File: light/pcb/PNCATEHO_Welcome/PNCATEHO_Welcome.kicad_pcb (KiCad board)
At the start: 2 copper layers, 85.6 x 54 mm, 53 parts, among them J1 USB_C_Receptacle_USB2.0, SW11 Boot, SW12 Reset, U1 RP2040, U2 RT9013-33GB, U3 W25Q32JVSSIQ, U4 USBLC6-2SC6, Y1 12MHz

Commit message: fix silc
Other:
- board text added: "pcb: turtle & inpudiy"
- board text removed: "pcb: turtle & inpdiy"

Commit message: add led
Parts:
- removed R8: 10k, PNCATEHO:R_0805_2012Metric_Pad1.20x1.40mm_HandSolder
- removed REF**: CreditCardPads, PNCATEHO:CreditCardPads
- added D10: LED_WS2812-2020, PNCATEHO:WS2812-2020-2.00mmx2.20mm, F.Cu at (156.6, 99.6)
- added D11: LED_WS2812-2020, PNCATEHO:WS2812-2020-2.00mmx2.20mm, F.Cu at (156.7, 116.7)
- added D12: LED_WS2812-2020, PNCATEHO:WS2812-2020-2.00mmx2.20mm, F.Cu at (173.7, 116.7)
- added D3: LED_WS2812-2020, PNCATEHO:WS2812-2020-2.00mmx2.20mm, F.Cu at (105.9, 82.8)
- added D4: LED_WS2812-2020, PNCATEHO:WS2812-2020-2.00mmx2.20mm, F.Cu at (122.8, 82.8)
- added D5: LED_WS2812-2020, PNCATEHO:WS2812-2020-2.00mmx2.20mm, F.Cu at (139.8, 82.8)
- added D6: LED_WS2812-2020, PNCATEHO:WS2812-2020-2.00mmx2.20mm, F.Cu at (156.7, 82.8)
- added D7: LED_WS2812-2020, PNCATEHO:WS2812-2020-2.00mmx2.20mm, F.Cu at (105.9, 99.8)
- added D8: LED_WS2812-2020, PNCATEHO:WS2812-2020-2.00mmx2.20mm, F.Cu at (122.8, 99.8)
- added D9: LED_WS2812-2020, PNCATEHO:WS2812-2020-2.00mmx2.20mm, F.Cu at (139.8, 99.8)
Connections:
- net /RP2040_D+ renamed Net-(U1-USB_DP)
- net /RP2040_D- renamed Net-(U1-USB_DM)
- net USB_PROTECTED_D+ renamed USB_DP
- net USB_PROTECTED_D- renamed USB_DM
- U1 pad 36: unconnected-(U1-GPIO24-Pad36) -> LED

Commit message: fix sh
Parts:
- D10, D11, D12, D3, D4, D5, D6, D7, D8, D9: value LED_WS2812-2020 -> ~
- moved D3 50.9 mm to (156.7, 82.8)
- moved D6 50.9 mm to (105.9, 82.8)
- moved D4 16.9 mm to (139.8, 82.8)
- moved D5 16.9 mm to (122.8, 82.8)
- moved D10 0.21 mm to (156.7, 99.8)
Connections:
- D11 pad 1: Net-(D10-DI) -> Net-(D11-DO)
- D11 pad 3: Net-(D11-DI) -> Net-(D10-DO)
- D12 pad 1: Net-(D11-DI) -> unconnected-(D12-DO-Pad1)
- D12 pad 3: unconnected-(D12-DI-Pad3) -> Net-(D11-DO)
- D3 pad 3: Net-(D3-DI) -> LED
- D4 pad 1: Net-(D3-DI) -> Net-(D4-DO)
- D4 pad 3: Net-(D4-DI) -> Net-(D3-DO)
- D5 pad 1: Net-(D4-DI) -> Net-(D5-DO)
- D5 pad 3: Net-(D5-DI) -> Net-(D4-DO)
- D6 pad 1: LED -> Net-(D6-DO)
- D6 pad 3: Net-(D3-DO) -> Net-(D5-DO)
- D7 pad 1: Net-(D5-DI) -> Net-(D7-DO)
- D7 pad 3: Net-(D7-DI) -> Net-(D6-DO)
- D8 pad 1: Net-(D7-DI) -> Net-(D8-DO)
- D8 pad 3: Net-(D8-DI) -> Net-(D7-DO)
- D9 pad 1: Net-(D8-DI) -> Net-(D10-DI)
- D9 pad 3: Net-(D10-DO) -> Net-(D8-DO)

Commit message: PNCATEHO Welcome RGB routing
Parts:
- moved D10 1.54 mm to (157.9, 100.7), turned to 180 degrees
- moved D11 1.54 mm to (157.9, 117.7), turned to 180 degrees
- moved D12 1.54 mm to (174.9, 117.7), turned to 180 degrees
- moved D3 1.54 mm to (157.9, 83.8), turned to 180 degrees
- moved D4 1.54 mm to (141.0, 83.8), turned to 180 degrees
- moved D5 1.54 mm to (124.0, 83.8), turned to 180 degrees
- moved D6 1.54 mm to (107.1, 83.8), turned to 180 degrees
- moved D7 1.54 mm to (107.1, 100.7), turned to 180 degrees
- moved D8 1.54 mm to (124.0, 100.7), turned to 180 degrees
- moved D9 1.54 mm to (141.0, 100.7), turned to 180 degrees
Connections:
- U1 pad 36: LED -> STATE_LED
- U1 pad 37: STATE_LED -> LED
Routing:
- net +5V: track 20.4 -> 219.6 mm, vias 0 -> 8
- net LED: track 0.00 -> 115.4 mm, vias 0 -> 2
- net Net-(D7-DO): track 0.00 -> 24.6 mm, vias 0 -> 2
- net Net-(D8-DO): track 0.00 -> 24.6 mm, vias 0 -> 2
- net Net-(D10-DI): track 0.00 -> 24.6 mm, vias 0 -> 2
- net Net-(D10-DO): track 0.00 -> 24.4 mm, vias 0 -> 2
- net Net-(D6-DO): track 0.00 -> 21.4 mm
- net Net-(D11-DO): track 0.00 -> 21.2 mm
- net Net-(D3-DO): track 0.00 -> 15.9 mm, vias 0 -> 2
- net Net-(D4-DO): track 0.00 -> 15.9 mm, vias 0 -> 2
- net Net-(D5-DO): track 0.00 -> 15.9 mm, vias 0 -> 2
- net ~{RESET}: track 77.2 -> 71.3 mm
- net R1C4: track 50.0 -> 53.2 mm

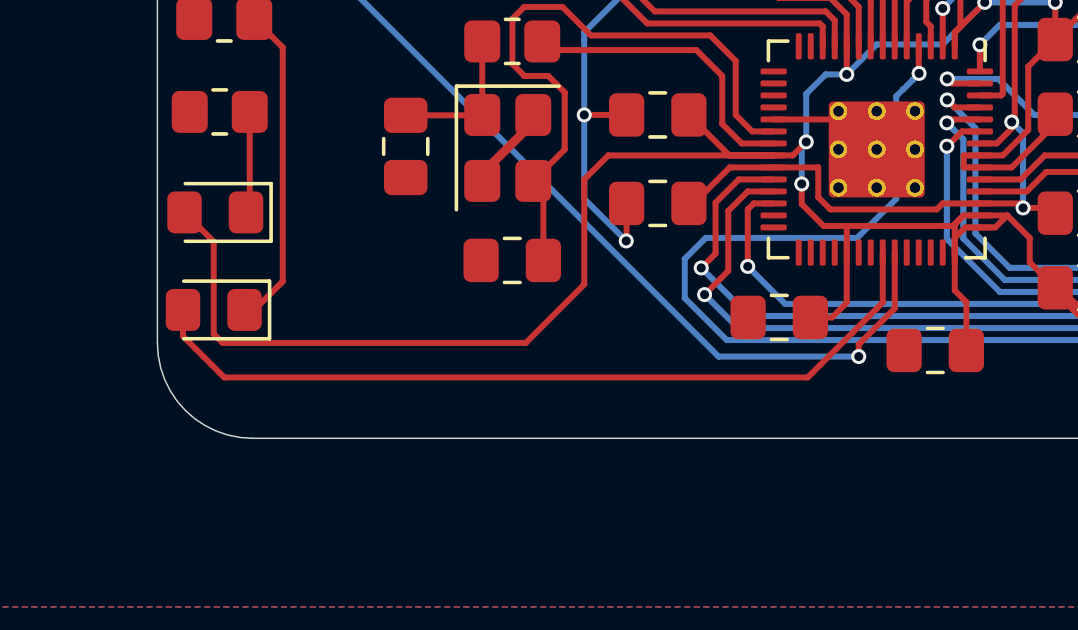
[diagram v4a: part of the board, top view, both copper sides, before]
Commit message: Return state led to GPIO25
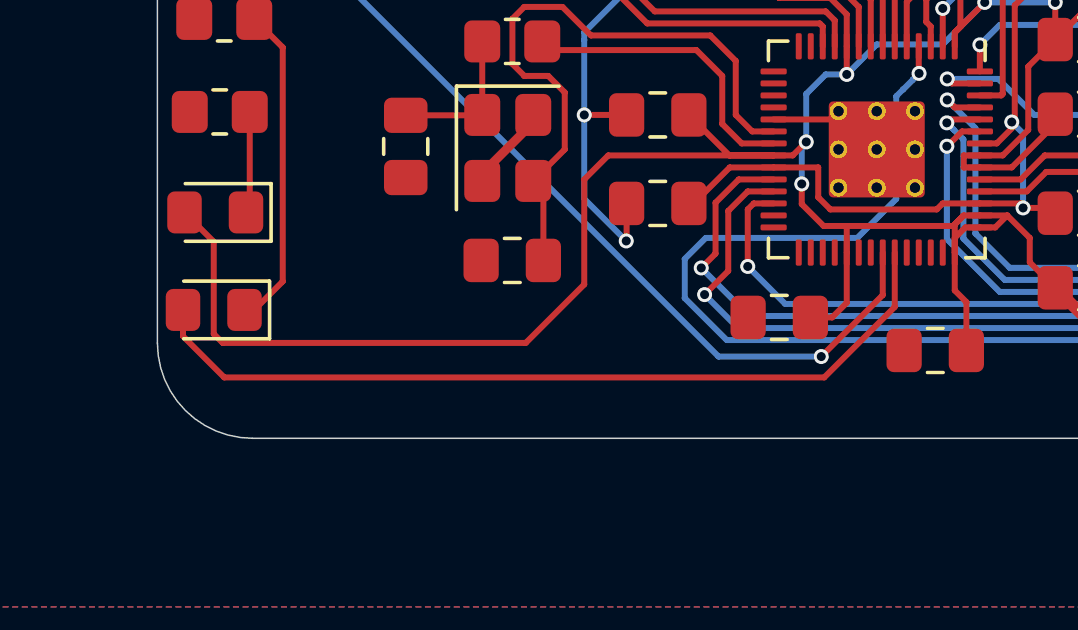
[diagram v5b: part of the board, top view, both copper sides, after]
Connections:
- U1 pad 36: STATE_LED -> LED
- U1 pad 37: LED -> STATE_LED
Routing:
- net LED: track 115.4 -> 114.5 mm

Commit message: update footprint
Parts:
- added G***: LOGO, PNCATEHO:Chip, F.Cu at (170.6, 98.7)
- added J2: Conn_01x10, PNCATEHO:JST_GH_SM10B-GHS-TB_1x10-1MP_P1.25mm_Horizontal, F.Cu at (139.3, 137.7)
- F1: footprint PNCATEHO:Fuse_0805_2012Metric -> PNCATEHO:Fuse_0805_2012Metric_Pad1.15x1.40mm_HandSolder
- TP1: footprint PNCATEHO:TestPoint_Pad_D2.0mm -> PNCATEHO:TestPoint_Pad_1.0x1.0mm
- TP2, TP3, TP4: footprint PNCATEHO:TestPoint_Pad_D2.0mm -> PNCATEHO:TestPoint_Pad_D1.0mm
- U1: footprint PNCATEHO:RP2040-QFN-56 -> PNCATEHO:QFN-56-1EP_7x7mm_P0.4mm_EP3.2x3.2mm_ThermalVias
- U2: footprint PNCATEHO:SOT-23-5_L3.0-W1.7-P0.95-LS2.8-BL -> PNCATEHO:SOT-23-5_HandSoldering
- U3: footprint PNCATEHO:SOIC127P790X216-8N -> PNCATEHO:SOIC-8_5.3x5.3mm_P1.27mm
- U4: footprint PNCATEHO:SOT-23-6_Handsoldering_REV -> PNCATEHO:SOT-23-6_Handsoldering
- Y1: footprint PNCATEHO:Crystal_SMD_3225-4Pin_3.2x2.5mm -> PNCATEHO:Crystal_SMD_3225-4Pin_3.2x2.5mm_HandSoldering
- moved C2 1.25 mm to (172.6, 99.2)
- moved R3 0.15 mm to (110.0, 116.8)
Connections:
- U1 pad 13: unconnected-(U1-GPIO10-Pad13) -> GPIO1
- U1 pad 14: unconnected-(U1-GPIO11-Pad14) -> GPIO2
- U1 pad 15: unconnected-(U1-GPIO12-Pad15) -> GPIO3
- U1 pad 16: unconnected-(U1-GPIO13-Pad16) -> GPIO4
- U1 pad 17: unconnected-(U1-GPIO14-Pad17) -> GPIO5
- U1 pad 18: unconnected-(U1-GPIO15-Pad18) -> GPIO6
- U1 pad 27: unconnected-(U1-GPIO16-Pad27) -> GPIO7
- U1 pad 28: unconnected-(U1-GPIO17-Pad28) -> GPIO8
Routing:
- net +3V3: track 196.1 -> 198.3 mm
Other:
- board text removed: "08/25"
- board text removed: "PWV: 020"
- board text removed: "VALID THRU"

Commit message: update pcb
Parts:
- added J3: Conn_01x10, PNCATEHO:JST_GH_SM10B-GHS-TB_1x10-1MP_P1.25mm_Horizontal, F.Cu at (84.5, 120.2)
- added J4: Conn_01x05, PNCATEHO:PinHeader_1x05_P2.54mm_Vertical, F.Cu at (73.0, 115.5)
- added J5: Conn_01x05, PNCATEHO:PinHeader_1x05_P2.54mm_Vertical, F.Cu at (77.6, 115.5)
- moved J2 48.9 mm to (93.6, 120.2), turned to -90 degrees
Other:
- board size 85.6 x 54 mm -> 114 x 54 mm
